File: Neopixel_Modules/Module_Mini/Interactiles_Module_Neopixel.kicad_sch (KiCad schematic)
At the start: 33 parts, among them J1 PINHD_1x2_Male, J2 PINHD_1x2_Female, J3 PINHD_1x2_Female, J4 PINHD_1x2_Female, J6 PINHD_1x2_Female, J8 PINHD_1x2_Female, U1 MCP23017_ML

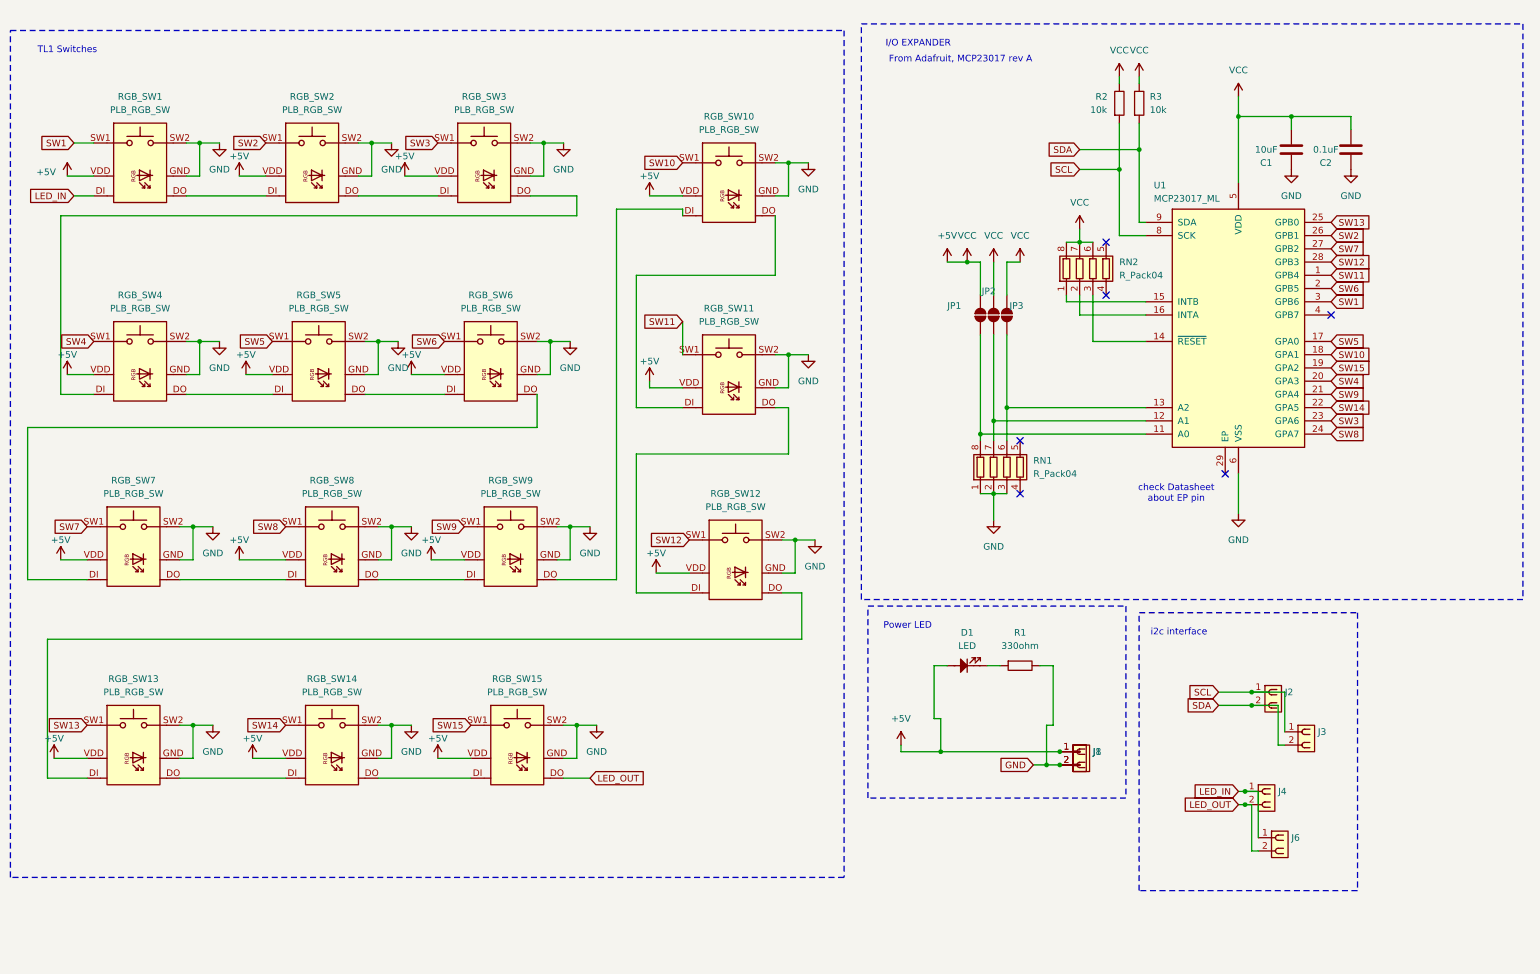
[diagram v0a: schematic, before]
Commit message: replaced picoblade connectors with THT pads, moved some stuff around
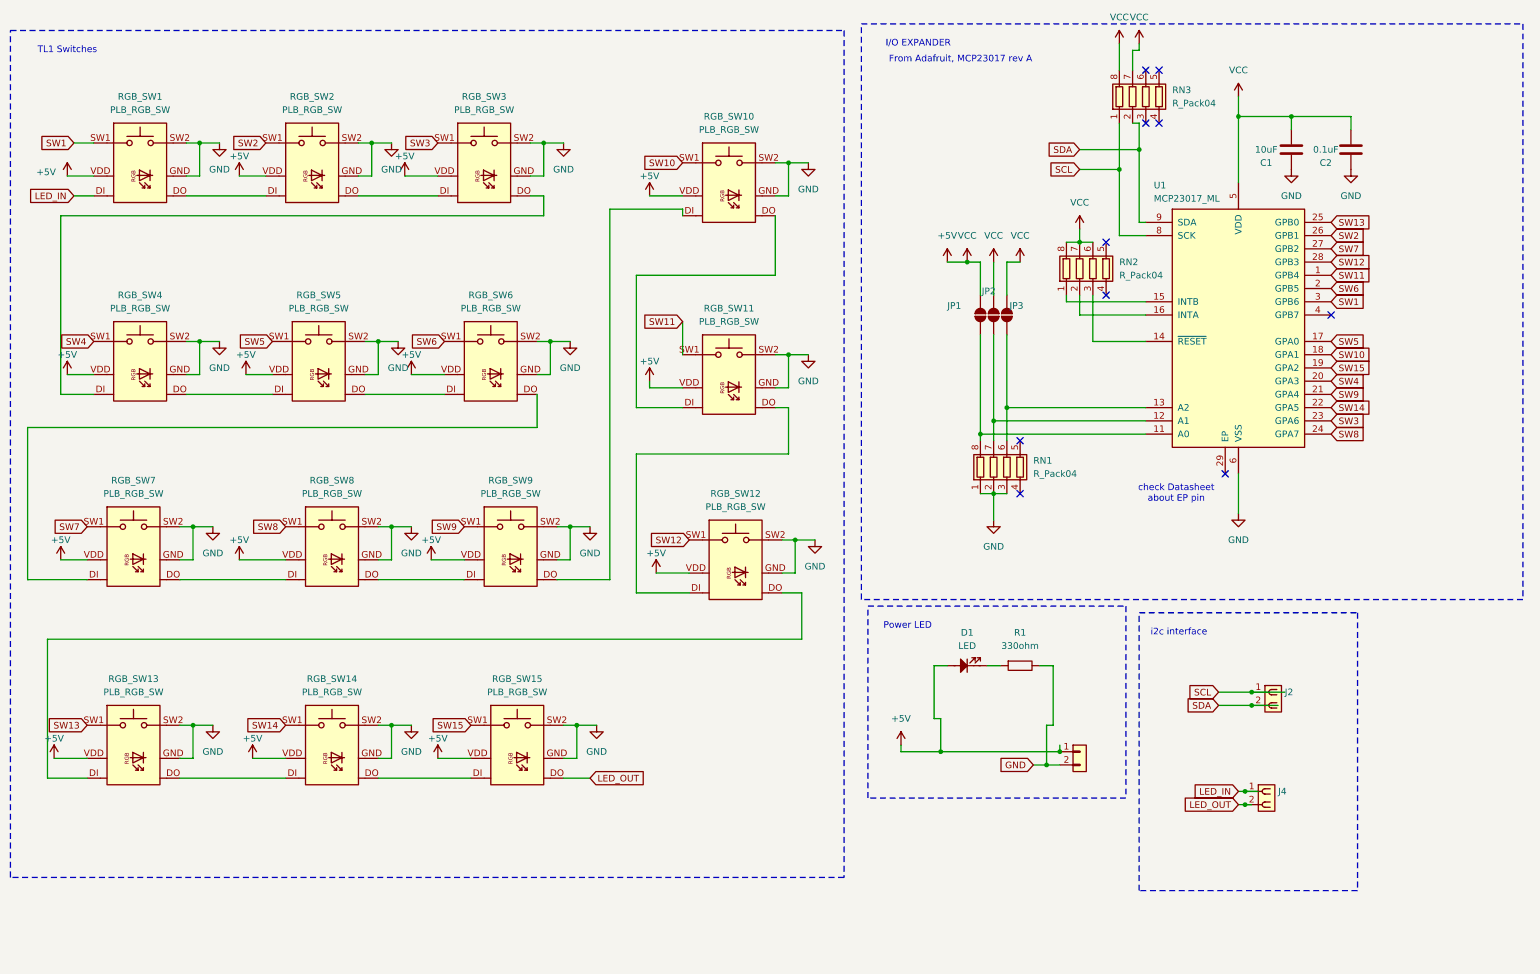
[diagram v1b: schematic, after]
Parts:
- removed J3, J6, J8: PINHD_1x2_Female, Connector_PinHeader_1.27mm:PinHeader_1x02_P1.27mm_Vertical, symbol PCM_SL_Pin_Headers:PINHD_1x2_Female
- removed R2, R3: 10k, Capacitor_SMD:C_0603_1608Metric_Pad1.08x0.95mm_HandSolder, symbol PCM_SL_Resistors:10k
- added RN3: R_Pack04, Resistor_SMD:R_Array_Convex_4x0603, symbol Device:R_Pack04
- J1, J2, J4: footprint Connector_Molex:Molex_PicoBlade_53261-0271_1x02-1MP_P1.25mm_Horizontal -> Connector_PinHeader_2.00mm:PinHeader_1x02_P2.00mm_Vertical
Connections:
- net +5V: now also RN3.7 (R2.2), RN3.8 (R1.2)
- net SCL: now also RN3.1 (R1.1)
- net SDA: now also RN3.2 (R2.1)
- no-connect marks 6 -> 10

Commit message: fixed for pcb production
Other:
- moved on the sheet: C1, C2, D1, J2, J4, JP1, JP2, JP3, R1, RN1, RN2, RN3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
